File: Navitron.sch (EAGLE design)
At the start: 78 parts, among them J2 DX07S016JA1R1500, Q1 ROHM_RUM002N02T2LROHM_RUM002N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, Q2 2.5A/30V, Q3 ROHM_RUM002N02T2LROHM_RUM002N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, Q4 ROHM_RUM002N02T2LROHM_RUM002N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, Q5 ROHM_RUM002N02T2LROHM_RUM002N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, T1 BC847, T2 BC847, U1 ESP32-WROOM-32, U2 9DoF IMU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

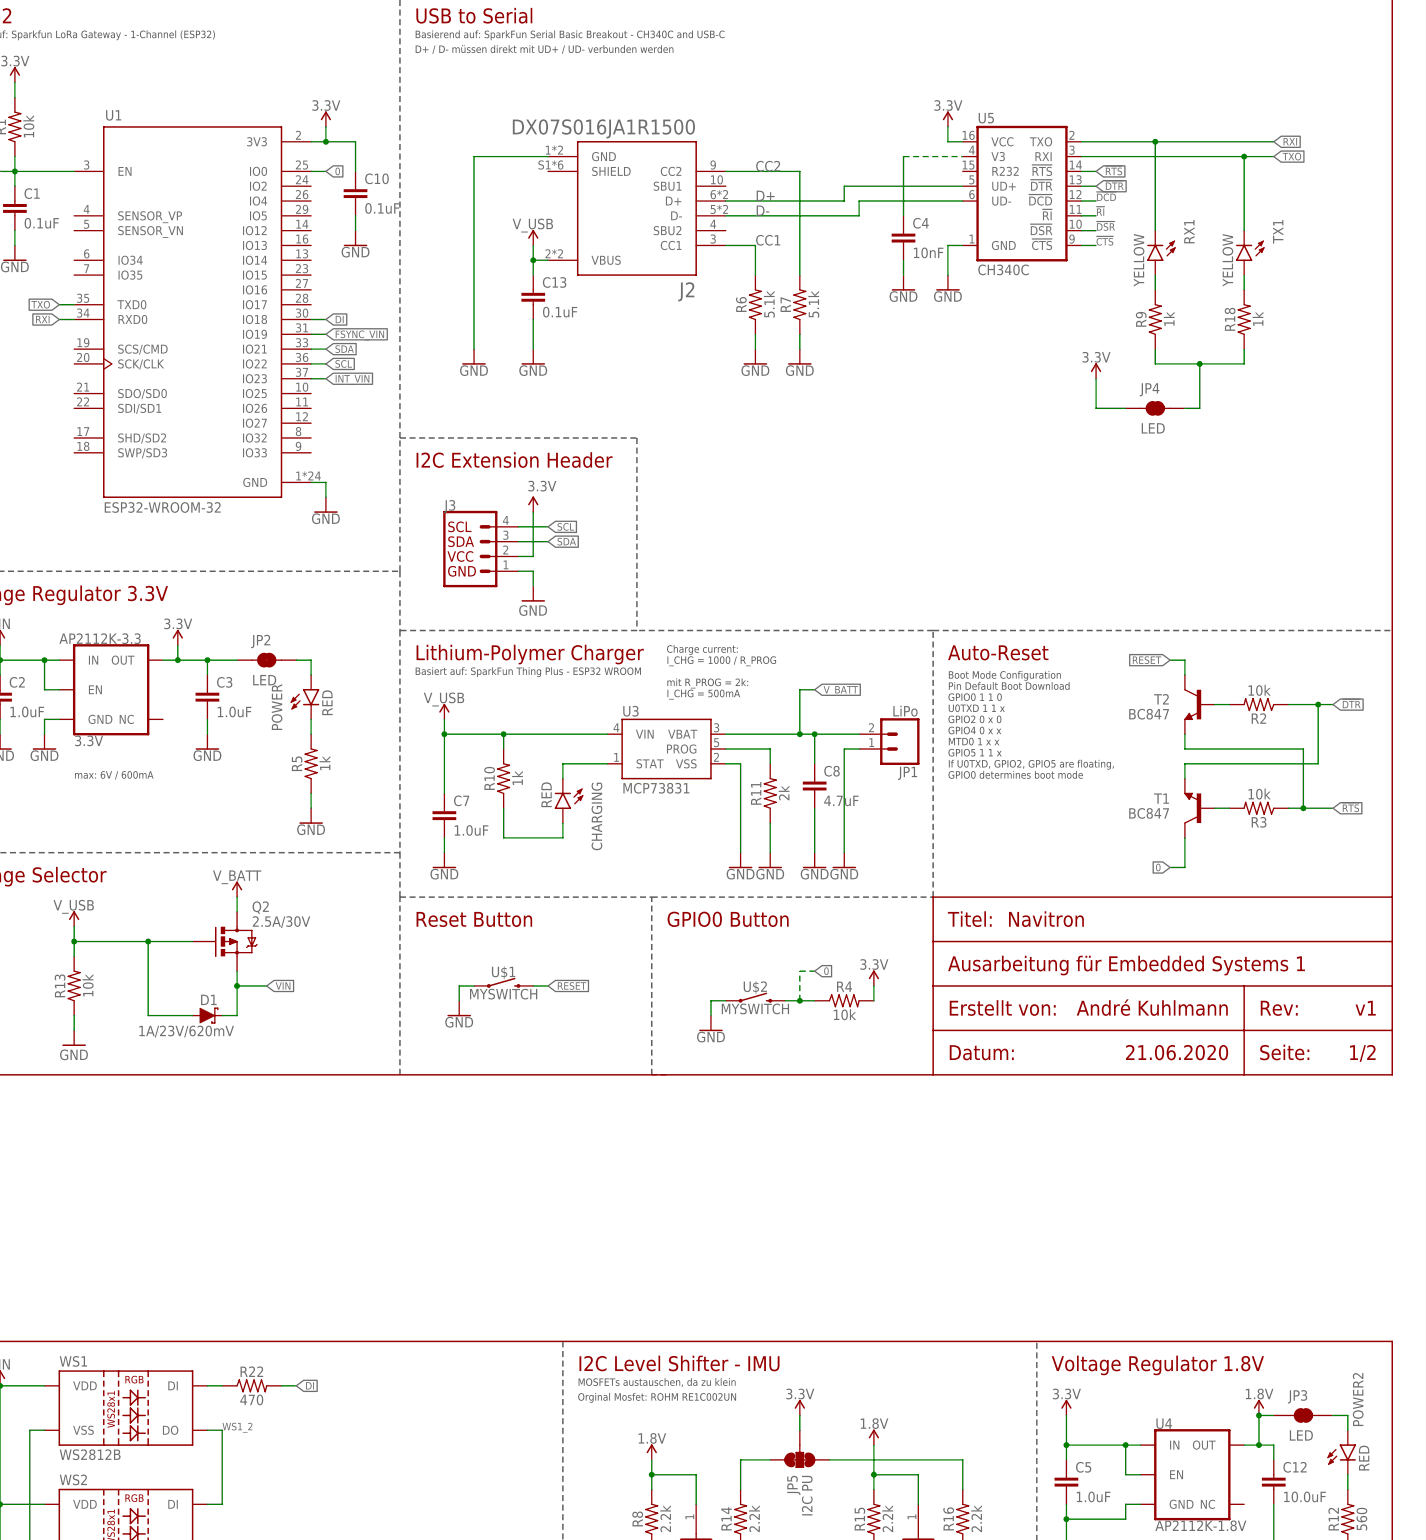
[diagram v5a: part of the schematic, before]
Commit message: Add Testingpoints
Added Testingpoints for:
- GND
- 3.3V
- 1.8V
- SDA
- SCL
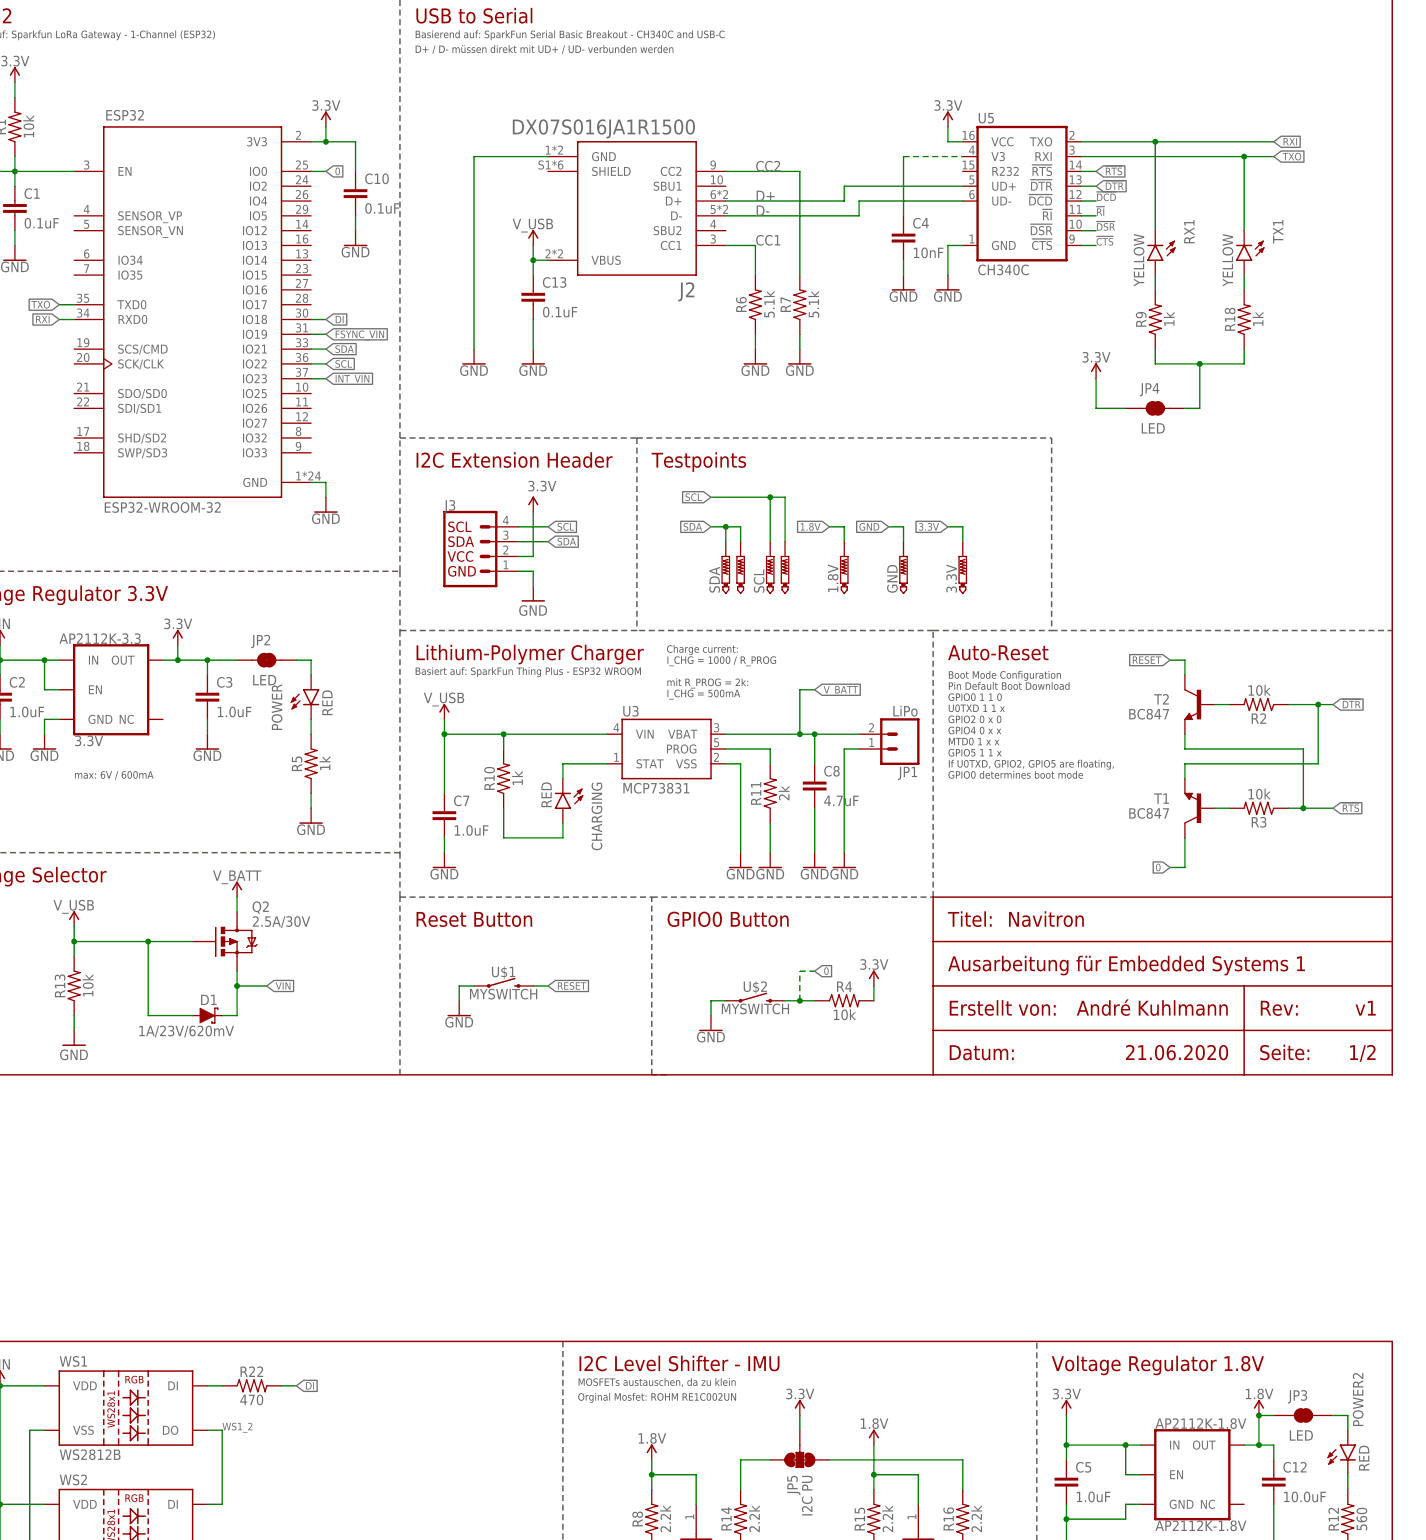
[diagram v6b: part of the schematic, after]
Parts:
- added 1.8V, 3.3V, GND, SCL, SCL1, SDA, SDA1: PTR1B1,27, testpad:PTR1B1,27
- renumbered U1 to ESP32, U4 to AP2112K-1.8V
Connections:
- net 1.8V: now also 1.8V.TP
- net 3.3V: now also 3.3V.TP
- net GND: now also GND.TP
- net SCL: now also SCL.TP, SCL1.TP
- net SDA: now also SDA.TP, SDA1.TP
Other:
- note added: "Testpoints"

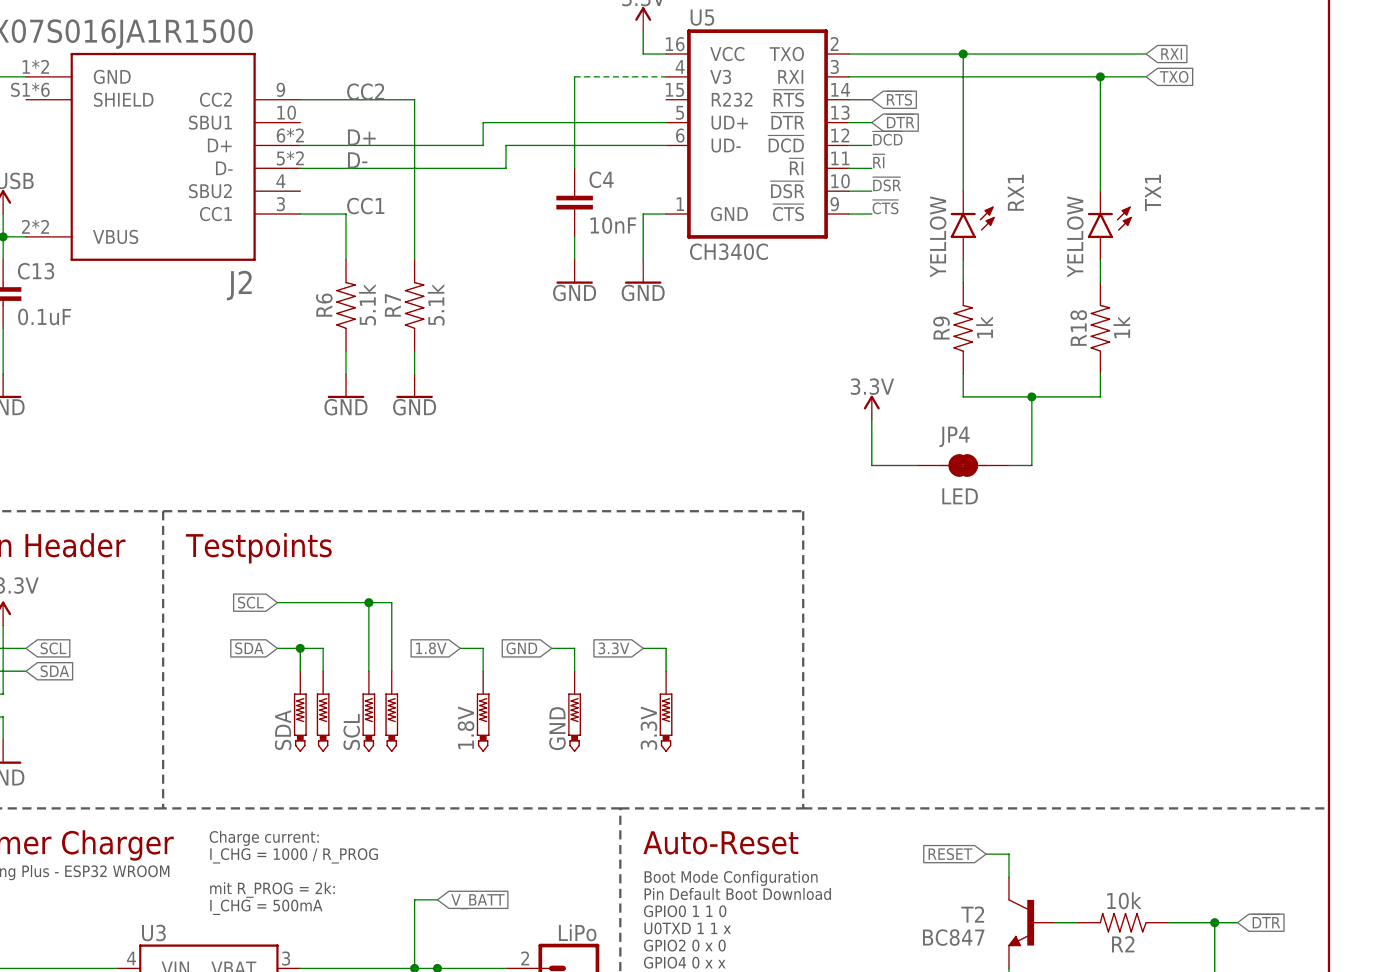
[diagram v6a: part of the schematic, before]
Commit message: Tented Vias + Some Changes
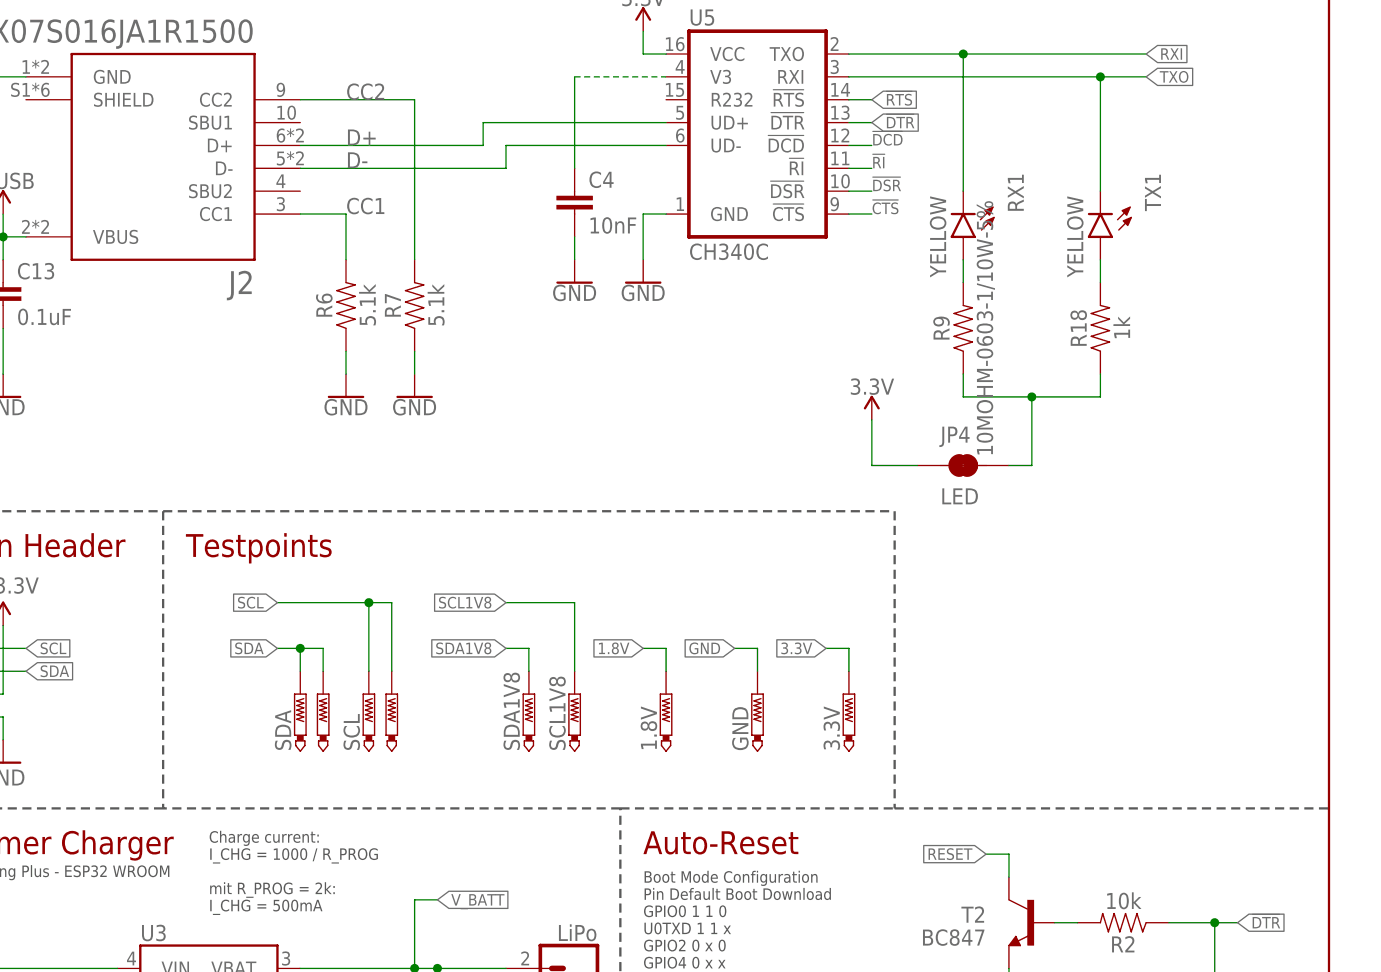
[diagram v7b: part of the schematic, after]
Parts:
- added SCL1V8, SDA1V8: PTR1B1,27, testpad:PTR1B1,27
- R9: value 1k -> 10MOHM-0603-1/10W-5%
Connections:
- net SCL1V8: now also SCL1V8.TP
- net SDA1V8: now also SDA1V8.TP
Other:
- moved on the sheet: 1.8V, 3.3V, GND
